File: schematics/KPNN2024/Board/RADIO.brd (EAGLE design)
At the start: 68.2 x 68.2 mm, 16 parts, among them J1 IPX-RADIO, J2 IPX-ANT

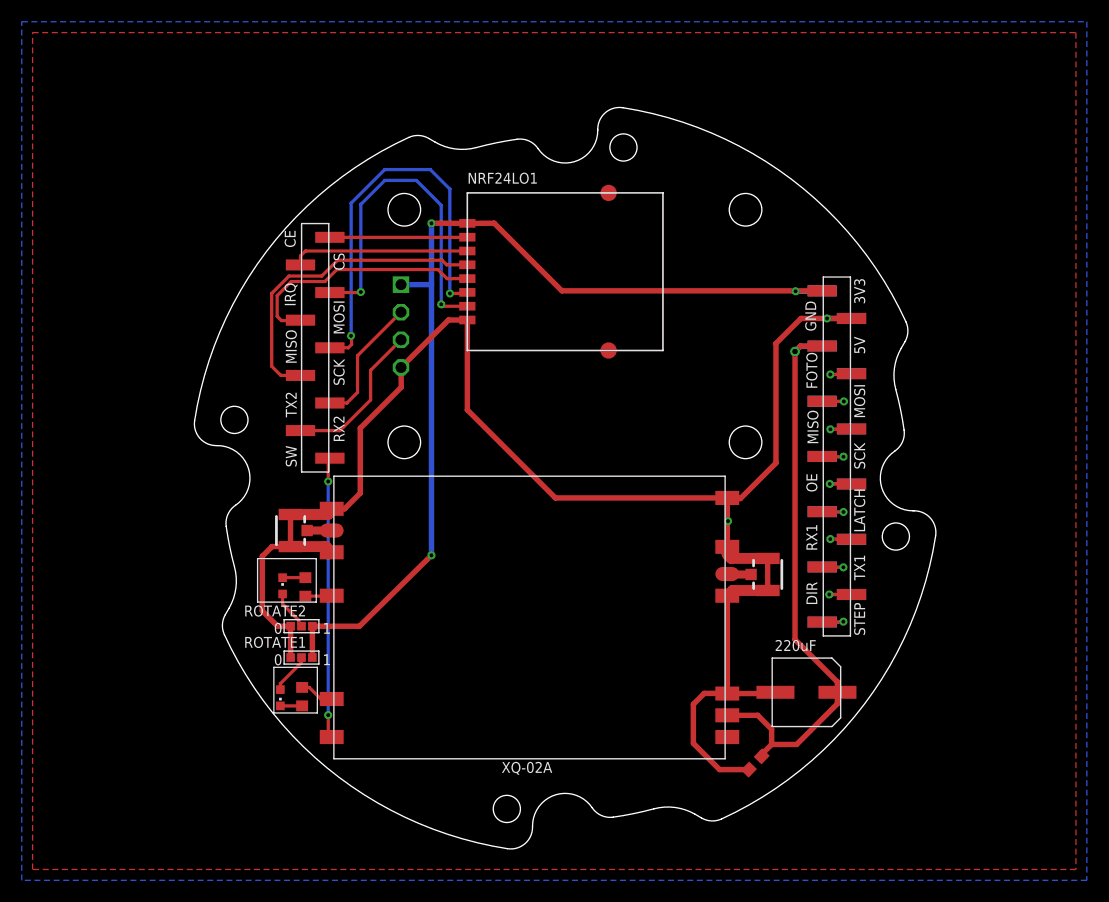
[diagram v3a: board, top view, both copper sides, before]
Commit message: Модели поправлены в соответствии с платами
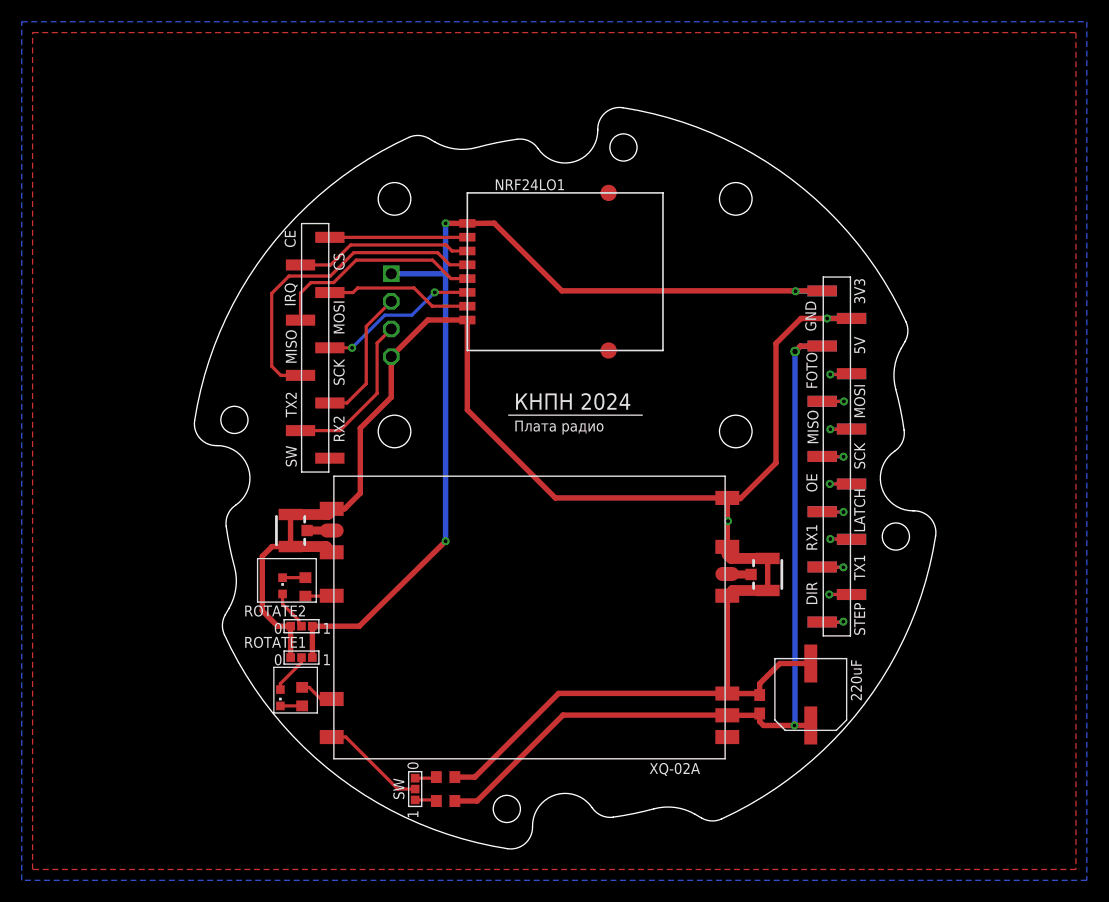
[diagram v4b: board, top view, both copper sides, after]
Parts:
- added R3, R4: 2k, rcl:R0603
- added SW: CONNECT_3, UNKNOWN-2024:CONNECT_3
- added U$1: Плата радио, UNKNOWN-2024:LOGO
- C2: device CanCubeSat:ECAP220-CMD -> UNKNOWN-2024:ECAP220-CMD
- moved C1 5.41 mm to (67.9, 29.2), turned to 270 degrees
- moved GPS-NEO7M 1.35 mm to (50.0, 65.0)
- moved C2 0.45 mm to (72.6, 30.1), turned to 180 degrees
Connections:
- removed net SW_WMP: U$7.9, XQ-02A.SW
- new net N$7: R3.2, SW.1
- new net N$8: R4.2, SW.3
- new net SW: SW.2, XQ-02A.SW
- net 5V: now also R3.1
- net GND: now also R4.1
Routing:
- net SW_WMP: track 25.9 -> 0.00 mm, vias 2 -> 0
- net MISO_RADIO: track 37.5 -> 14.8 mm
- net 5V: track 54.5 -> 76.8 mm, vias 1 -> 2
- net GND: track 160.7 -> 181.9 mm
- net IRQ_RADIO: track 31.8 -> 13.5 mm, vias 2 -> 0
- net SW: track 0.00 -> 9.66 mm
- net MOSI_RADIO: track 23.1 -> 19.8 mm
- net N$8: track 0.00 -> 1.99 mm
- net N$7: track 0.00 -> 1.99 mm
- net 3V3: track 91.0 -> 92.3 mm
- net RX2_GPS: track 14.3 -> 14.9 mm
- net TX2_GPS: track 12.0 -> 12.6 mm
- net SCK_RADIO: track 29.1 -> 29.7 mm
